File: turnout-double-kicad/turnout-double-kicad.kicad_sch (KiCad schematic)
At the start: 23 parts

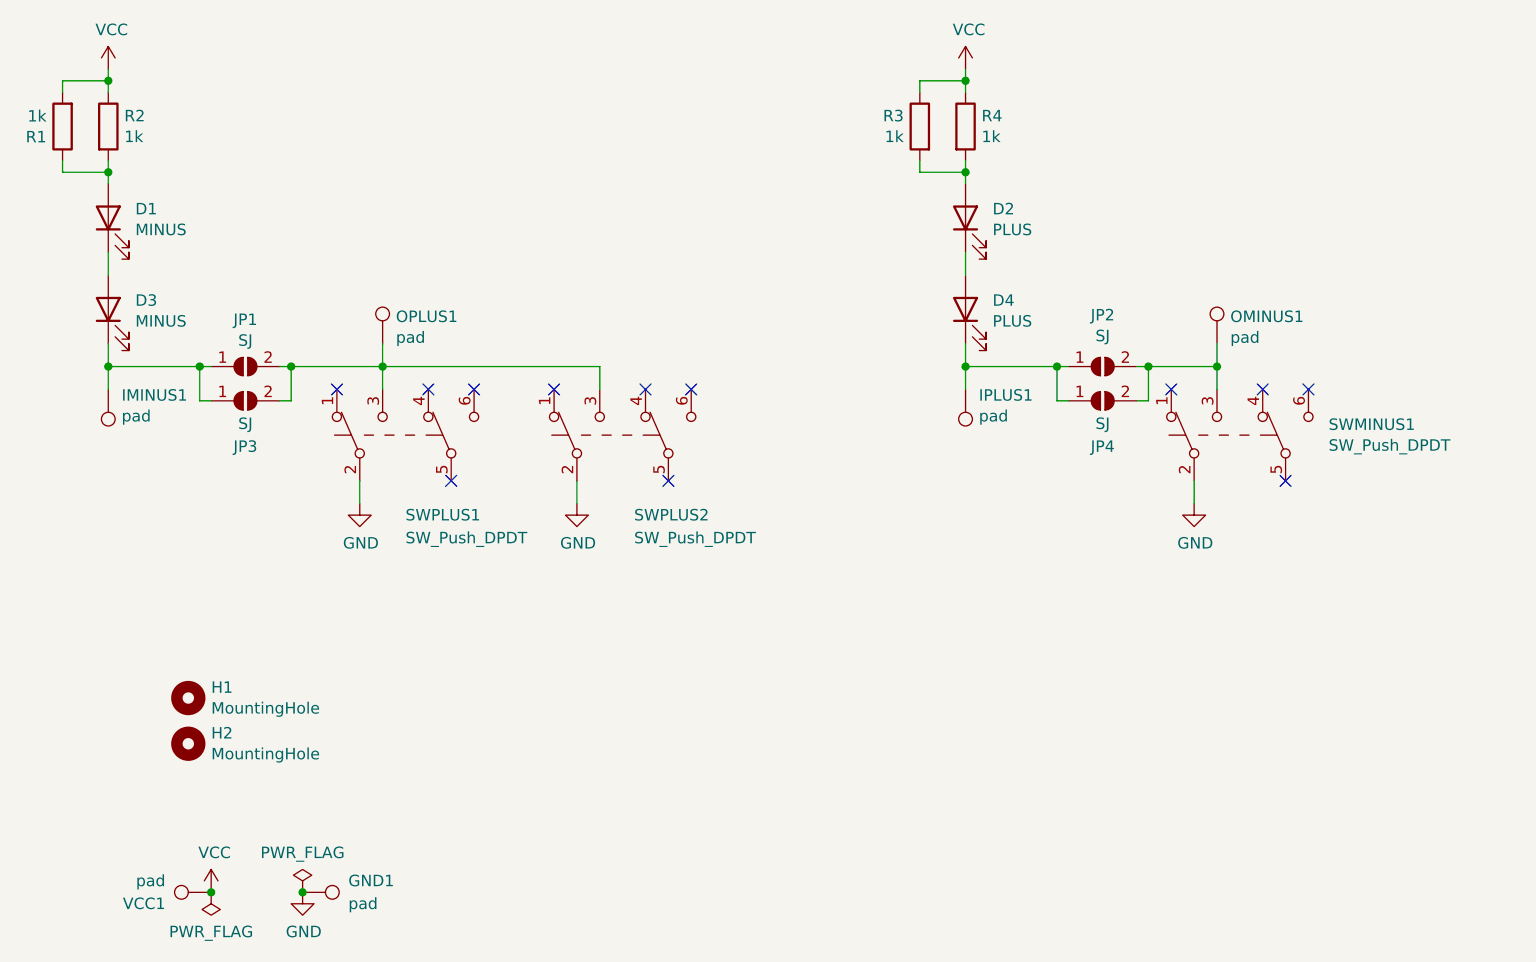
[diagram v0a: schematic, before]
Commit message: turnout-double: add wires for reversed placing.
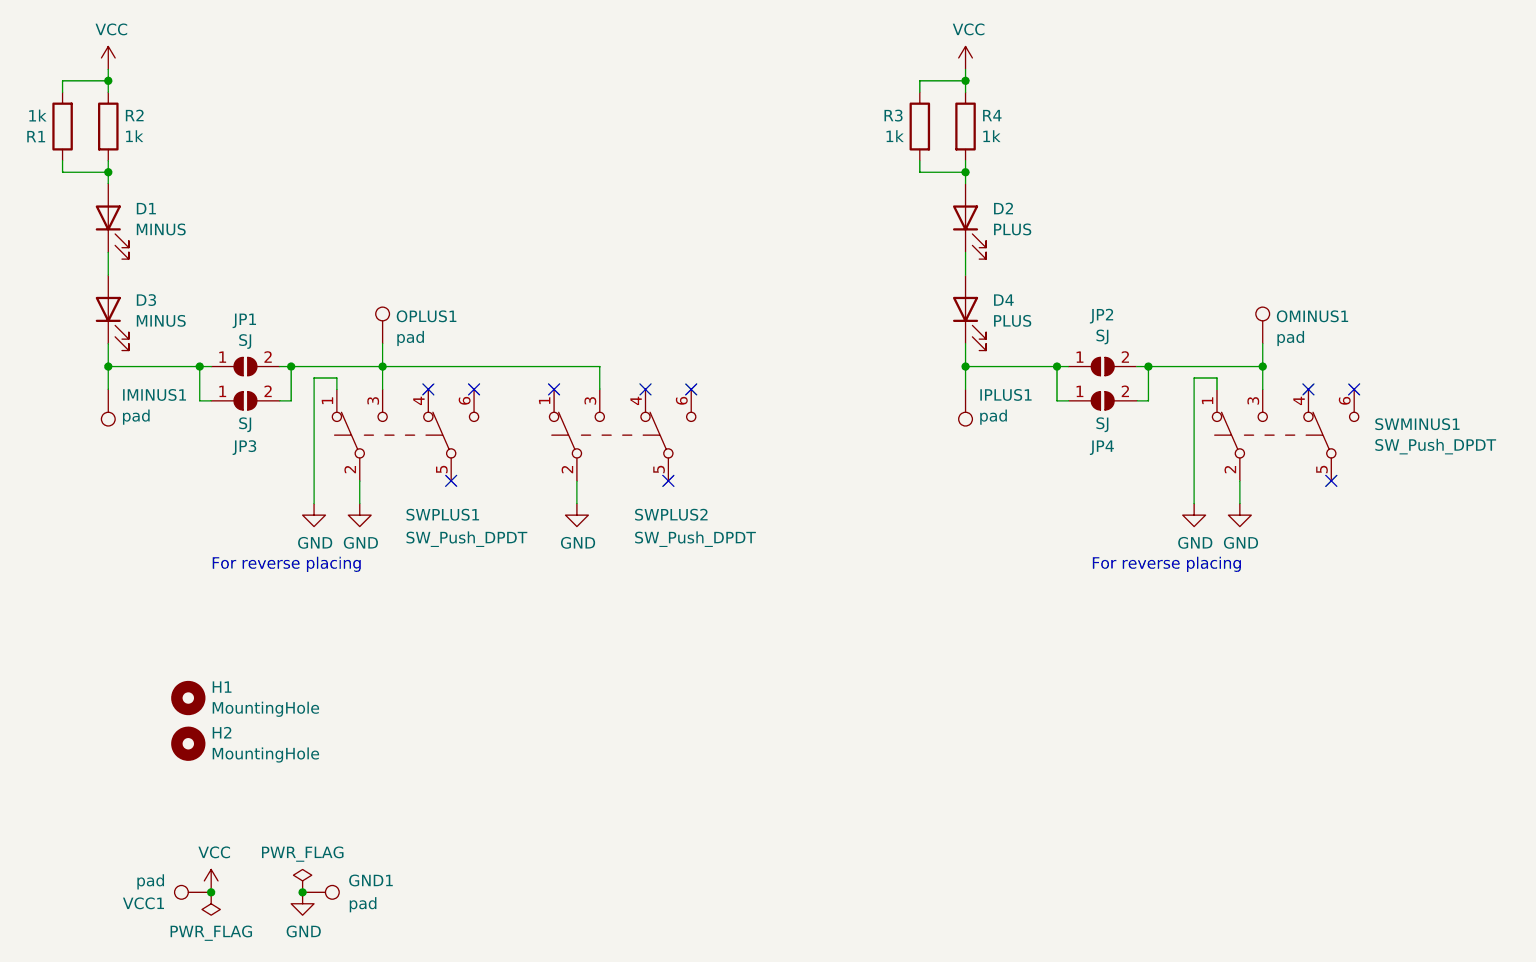
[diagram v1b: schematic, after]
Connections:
- net GND: now also SWMINUS1.1 (A), SWPLUS1.1 (A)
- no-connect marks 12 -> 10
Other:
- note added: "For reverse placing"
- moved on the sheet: OMINUS1, SWMINUS1
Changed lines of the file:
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@@
     (title "Manual panel control double turnout")
     (date "2021-11-10")
+    (rev "3.0")
   )
   (junction (at 125.73 63.5) (diameter 0) (color 0 0 0 0)
@@
   (junction (at 40.64 63.5) (diameter 0) (color 0 0 0 0)
   )
-  (junction (at 153.67 63.5) (diameter 0) (color 0 0 0 0)
-  )
   (junction (at 30.48 31.75) (diameter 0) (color 0 0 0 0)
   )
@@
   )
   (junction (at 41.91 121.92) (diameter 0) (color 0 0 0 0)
+  )
+  (junction (at 158.75 63.5) (diameter 0) (color 0 0 0 0)
   )
   (junction (at 125.73 31.75) (diameter 0) (color 0 0 0 0)
@@
   (no_connect (at 68.58 76.2))
   (no_connect (at 66.04 66.04))
-  (no_connect (at 148.59 66.04))
   (no_connect (at 95.25 66.04))
-  (no_connect (at 161.29 76.2))
+  (no_connect (at 166.37 76.2))
   (no_connect (at 92.71 76.2))
   (no_connect (at 90.17 66.04))
-  (no_connect (at 158.75 66.04))
+  (no_connect (at 163.83 66.04))
   (no_connect (at 80.01 66.04))
-  (no_connect (at 163.83 66.04))
-  (no_connect (at 55.88 66.04))
+  (no_connect (at 168.91 66.04))
   (wire (pts (xy 30.48 50.8) (xy 30.48 53.34))
     (stroke (width 0) (type default) (color 0 0 0 0))
@@
     (stroke (width 0) (type default) (color 0 0 0 0))
   )
-  (wire (pts (xy 153.67 63.5) (xy 146.05 63.5))
+  (wire (pts (xy 146.05 63.5) (xy 158.75 63.5))
     (stroke (width 0) (type default) (color 0 0 0 0))
   )
@@
     (stroke (width 0) (type default) (color 0 0 0 0))
   )
+  (wire (pts (xy 153.67 64.77) (xy 151.13 64.77))
+    (stroke (width 0) (type default) (color 0 0 0 0))
+  )
+  (wire (pts (xy 158.75 63.5) (xy 158.75 66.04))
+    (stroke (width 0) (type default) (color 0 0 0 0))
+  )
   (wire (pts (xy 30.48 60.96) (xy 30.48 63.5))
     (stroke (width 0) (type default) (color 0 0 0 0))
@@
     (stroke (width 0) (type default) (color 0 0 0 0))
   )
+  (wire (pts (xy 151.13 64.77) (xy 151.13 78.74))
+    (stroke (width 0) (type default) (color 0 0 0 0))
+  )
   (wire (pts (xy 82.55 78.74) (xy 82.55 76.2))
     (stroke (width 0) (type default) (color 0 0 0 0))
   )
+  (wire (pts (xy 53.34 78.74) (xy 53.34 64.77))
+    (stroke (width 0) (type default) (color 0 0 0 0))
+  )
+  (wire (pts (xy 53.34 64.77) (xy 55.88 64.77))
+    (stroke (width 0) (type default) (color 0 0 0 0))
+  )
   (wire (pts (xy 41.91 63.5) (xy 40.64 63.5))
     (stroke (width 0) (type default) (color 0 0 0 0))
@@
     (stroke (width 0) (type default) (color 0 0 0 0))
   )
+  (wire (pts (xy 153.67 66.04) (xy 153.67 64.77))
+    (stroke (width 0) (type default) (color 0 0 0 0))
+  )
   (wire (pts (xy 146.05 63.5) (xy 144.78 63.5))
     (stroke (width 0) (type default) (color 0 0 0 0))
   )
-  (wire (pts (xy 151.13 76.2) (xy 151.13 78.74))
+  (wire (pts (xy 156.21 76.2) (xy 156.21 78.74))
     (stroke (width 0) (type default) (color 0 0 0 0))
   )
@@
     (stroke (width 0) (type default) (color 0 0 0 0))
   )
-  (wire (pts (xy 153.67 63.5) (xy 153.67 66.04))
+  (wire (pts (xy 158.75 60.96) (xy 158.75 63.5))
     (stroke (width 0) (type default) (color 0 0 0 0))
   )
@@
     (stroke (width 0) (type default) (color 0 0 0 0))
   )
-  (wire (pts (xy 153.67 60.96) (xy 153.67 63.5))
+  (wire (pts (xy 55.88 64.77) (xy 55.88 66.04))
     (stroke (width 0) (type default) (color 0 0 0 0))
   )
   (wire (pts (xy 50.8 67.31) (xy 50.8 63.5))
     (stroke (width 0) (type default) (color 0 0 0 0))
+  )
+  (text "For reverse placing" (at 41.91 86.36 0)
+    (effects (font (size 1.27 1.27)) (justify left bottom))
+  )
+  (text "For reverse placing" (at 139.7 86.36 0)
+    (effects (font (size 1.27 1.27)) (justify left bottom))
   )
   (symbol (lib_id "power:GND") (at 58.42 78.74 0) (unit 1)
@@
     (pin "1")
   )
-  (symbol (lib_id "power:GND") (at 151.13 78.74 0) (unit 1)
-    (in_bom yes) (on_board yes)
-    (property "Reference" "#PWR05" (id 0) (at 151.13 85.09 0)
-      (effects (font (size 1.27 1.27)) hide)
-    )
-    (property "Value" "GND" (id 1) (at 151.257 83.1342 0))
-    (property "Footprint" "" (id 2) (at 151.13 78.74 0)
-      (effects (font (size 1.27 1.27)) hide)
-    )
-    (property "Datasheet" "" (id 3) (at 151.13 78.74 0)
-      (effects (font (size 1.27 1.27)) hide)
-    )
-    (pin "1")
-  )
-  (symbol (lib_id "Connector:TestPoint") (at 153.67 60.96 0) (unit 1)
-    (in_bom yes) (on_board yes)
-    (property "Reference" "OMINUS1" (id 0) (at 155.1432 57.9628 0)
-      (effects (font (size 1.27 1.27)) (justify left))
-    )
-    (property "Value" "pad" (id 1) (at 155.1432 60.2742 0)
-      (effects (font (size 1.27 1.27)) (justify left))
-    )
-    (property "Footprint" "Connector_Pin:Pin_D1.3mm_L11.0mm" (id 2) (at 158.75 60.96 0)
-      (effects (font (size 1.27 1.27)) hide)
-    )
-    (property "Datasheet" "~" (id 3) (at 158.75 60.96 0)
-      (effects (font (size 1.27 1.27)) hide)
-    )
-    (pin "1")
-  )
-  (symbol (lib_id "Switch:SW_Push_DPDT") (at 156.21 71.12 90) (unit 1)
-    (in_bom yes) (on_board yes)
-    (property "Reference" "SWMINUS1" (id 0) (at 166.0652 69.9516 90)
-      (effects (font (size 1.27 1.27)) (justify right))
-    )
-    (property "Value" "SW_Push_DPDT" (id 1) (at 166.0652 72.263 90)
-      (effects (font (size 1.27 1.27)) (justify right))
-    )
-    (property "Footprint" "Switch_KMZ:KLS7" (id 2) (at 151.13 71.12 0)
-      (effects (font (size 1.27 1.27)) hide)
-    )
-    (property "Datasheet" "~" (id 3) (at 151.13 71.12 0)
+  (symbol (lib_id "power:GND") (at 156.21 78.74 0) (unit 1)
+    (in_bom yes) (on_board yes)
+    (property "Reference" "#PWR05" (id 0) (at 156.21 85.09 0)
+      (effects (font (size 1.27 1.27)) hide)
+    )
+    (property "Value" "GND" (id 1) (at 156.337 83.1342 0))
+    (property "Footprint" "" (id 2) (at 156.21 78.74 0)
+      (effects (font (size 1.27 1.27)) hide)
+    )
+    (property "Datasheet" "" (id 3) (at 156.21 78.74 0)
+      (effects (font (size 1.27 1.27)) hide)
+    )
+    (pin "1")
+  )
+  (symbol (lib_id "Connector:TestPoint") (at 158.75 60.96 0) (unit 1)
+    (in_bom yes) (on_board yes)
+    (property "Reference" "OMINUS1" (id 0) (at 160.2232 57.9628 0)
+      (effects (font (size 1.27 1.27)) (justify left))
+    )
+    (property "Value" "pad" (id 1) (at 160.2232 60.2742 0)
+      (effects (font (size 1.27 1.27)) (justify left))
+    )
+    (property "Footprint" "Connector_Pin:Pin_D1.3mm_L11.0mm" (id 2) (at 163.83 60.96 0)
+      (effects (font (size 1.27 1.27)) hide)
+    )
+    (property "Datasheet" "~" (id 3) (at 163.83 60.96 0)
+      (effects (font (size 1.27 1.27)) hide)
+    )
+    (pin "1")
+  )
+  (symbol (lib_id "Switch:SW_Push_DPDT") (at 161.29 71.12 90) (unit 1)
+    (in_bom yes) (on_board yes)
+    (property "Reference" "SWMINUS1" (id 0) (at 171.1452 69.9516 90)
+      (effects (font (size 1.27 1.27)) (justify right))
+    )
+    (property "Value" "SW_Push_DPDT" (id 1) (at 171.1452 72.263 90)
+      (effects (font (size 1.27 1.27)) (justify right))
+    )
+    (property "Footprint" "Switch_KMZ:KLS7" (id 2) (at 156.21 71.12 0)
+      (effects (font (size 1.27 1.27)) hide)
+    )
+    (property "Datasheet" "~" (id 3) (at 156.21 71.12 0)
       (effects (font (size 1.27 1.27)) hide)
     )
@@
     (pin "2")
   )
+  (symbol (lib_id "power:GND") (at 53.34 78.74 0) (unit 1)
+    (in_bom yes) (on_board yes)
+    (property "Reference" "#PWR0102" (id 0) (at 53.34 85.09 0)
+      (effects (font (size 1.27 1.27)) hide)
+    )
+    (property "Value" "GND" (id 1) (at 53.467 83.1342 0))
+    (property "Footprint" "" (id 2) (at 53.34 78.74 0)
+      (effects (font (size 1.27 1.27)) hide)
+    )
+    (property "Datasheet" "" (id 3) (at 53.34 78.74 0)
+      (effects (font (size 1.27 1.27)) hide)
+    )
+    (pin "1")
+  )
+  (symbol (lib_id "power:GND") (at 151.13 78.74 0) (unit 1)
+    (in_bom yes) (on_board yes)
+    (property "Reference" "#PWR0101" (id 0) (at 151.13 85.09 0)
+      (effects (font (size 1.27 1.27)) hide)
+    )
+    (property "Value" "GND" (id 1) (at 151.257 83.1342 0))
+    (property "Footprint" "" (id 2) (at 151.13 78.74 0)
+      (effects (font (size 1.27 1.27)) hide)
+    )
+    (property "Datasheet" "" (id 3) (at 151.13 78.74 0)
+      (effects (font (size 1.27 1.27)) hide)
+    )
+    (pin "1")
+  )
   (sheet_instances
     (path "/" (page "1"))
@@
       (reference "#PWR07") (unit 1) (value "GND") (footprint "")
     )
+    (path "/eedd9ced-511f-4823-9bd3-3e531e07c6db"
+      (reference "#PWR0101") (unit 1) (value "GND") (footprint "")
+    )
+    (path "/7bf7143e-fc31-4003-beba-ef82b91e326c"
+      (reference "#PWR0102") (unit 1) (value "GND") (footprint "")
+    )
     (path "/00000000-0000-0000-0000-0000618b7099"
